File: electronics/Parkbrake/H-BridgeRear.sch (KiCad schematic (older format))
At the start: 82 parts

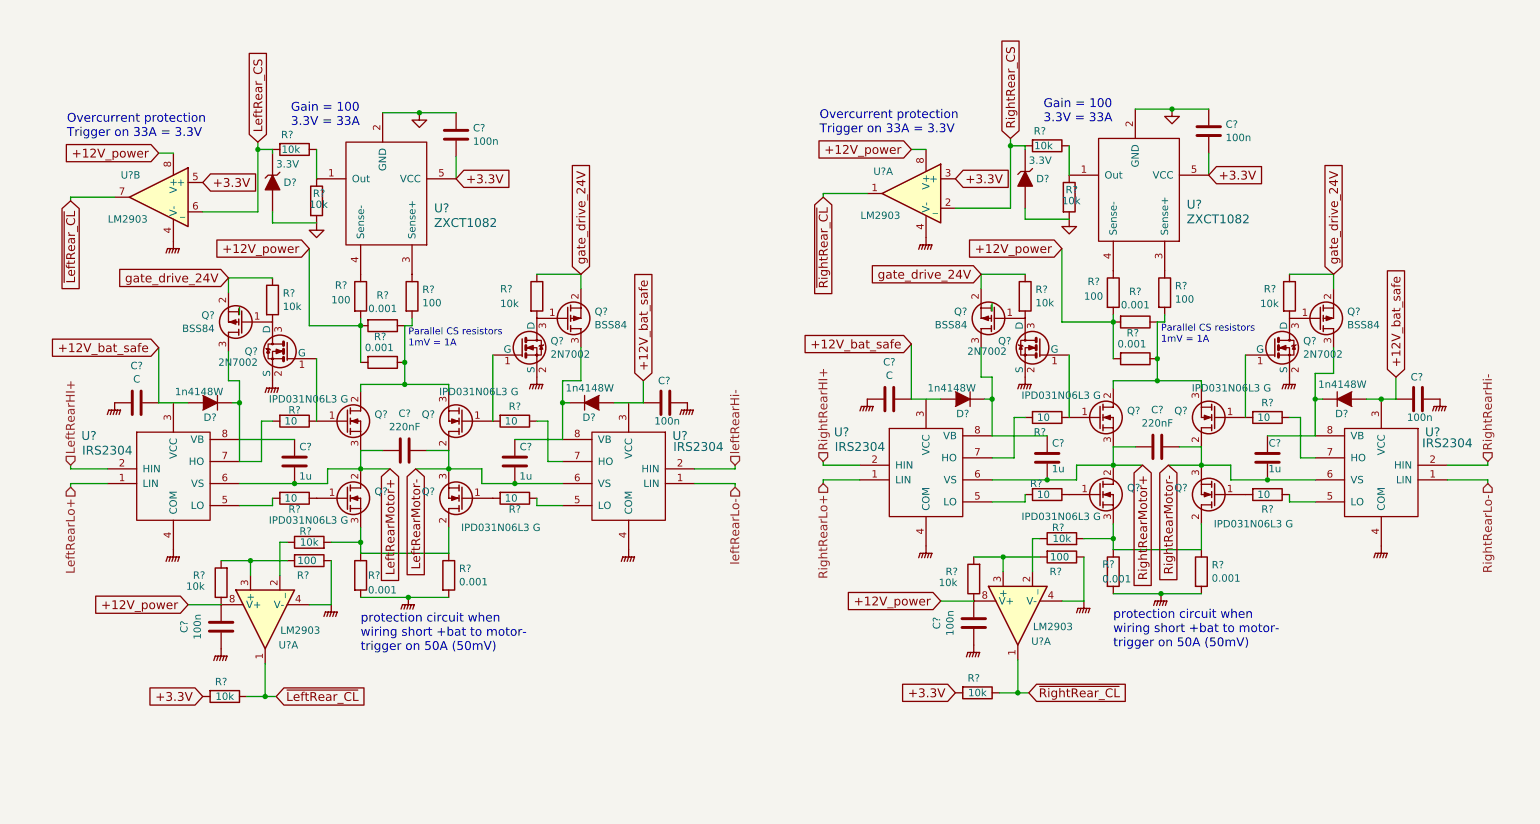
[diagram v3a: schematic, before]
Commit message: ordernr, type and footprints for all components
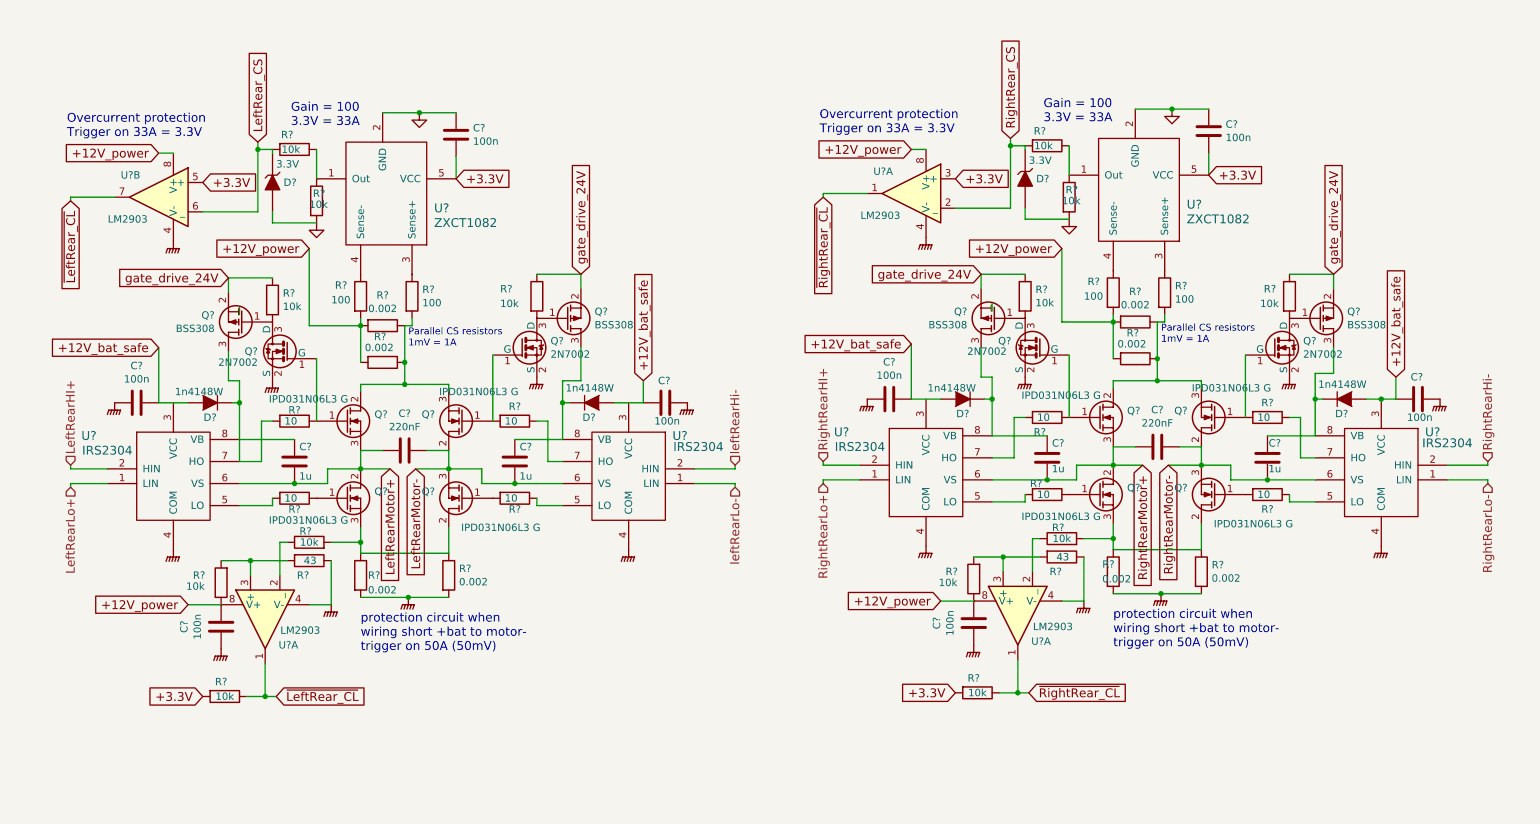
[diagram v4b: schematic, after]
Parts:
- C? (x2): footprint (none) -> Capacitors_SMD:C_1206; farnell (none) -> 2497088; part (none) -> 1206B224J500CT
- C? (x6): footprint (none) -> Capacitors_SMD:C_0805; farnell (none) -> 2496940; part (none) -> 0805B104J500CT
- C? (x4): footprint (none) -> Capacitors_SMD:C_1206; farnell (none) -> 2362126; part (none) -> GRM31MR71E105JA01L
- C? (x2): value C -> 100n; footprint (none) -> Capacitors_SMD:C_0805; farnell (none) -> 2496940; part (none) -> 0805B104J500CT
- D? (x4): footprint (none) -> Diodes_SMD:SOD-123; farnell (none) -> 2433353; part (none) -> 1N4148W-E3-08
- D? (x2): footprint (none) -> Diodes_SMD:SOD-123; farnell (none) -> 2454044; part (none) -> MMSZ4684
- Q? (x4): footprint (none) -> TO_SOT_Packages_SMD:TO-252-2Lead
- Q? (x4): footprint TO_SOT_Packages_SMD:SOT-23_Handsoldering -> TO_SOT_Packages_SMD:SOT-23
- Q? (x4): value BSS84 -> BSS308; footprint TO_SOT_Packages_SMD:SOT-23_Handsoldering -> TO_SOT_Packages_SMD:SOT-23; farnell 1510765 -> 2432719; part BSS84 -> BSS308PE H6327
- R? (x8): value 0.001 -> 0.002
- R? (x2): value 100 -> 43; footprint (none) -> Resistors_SMD:R_0805; farnell (none) -> 9333240; part (none) -> MC01W0805143R

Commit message: Make it pass DRC rule check
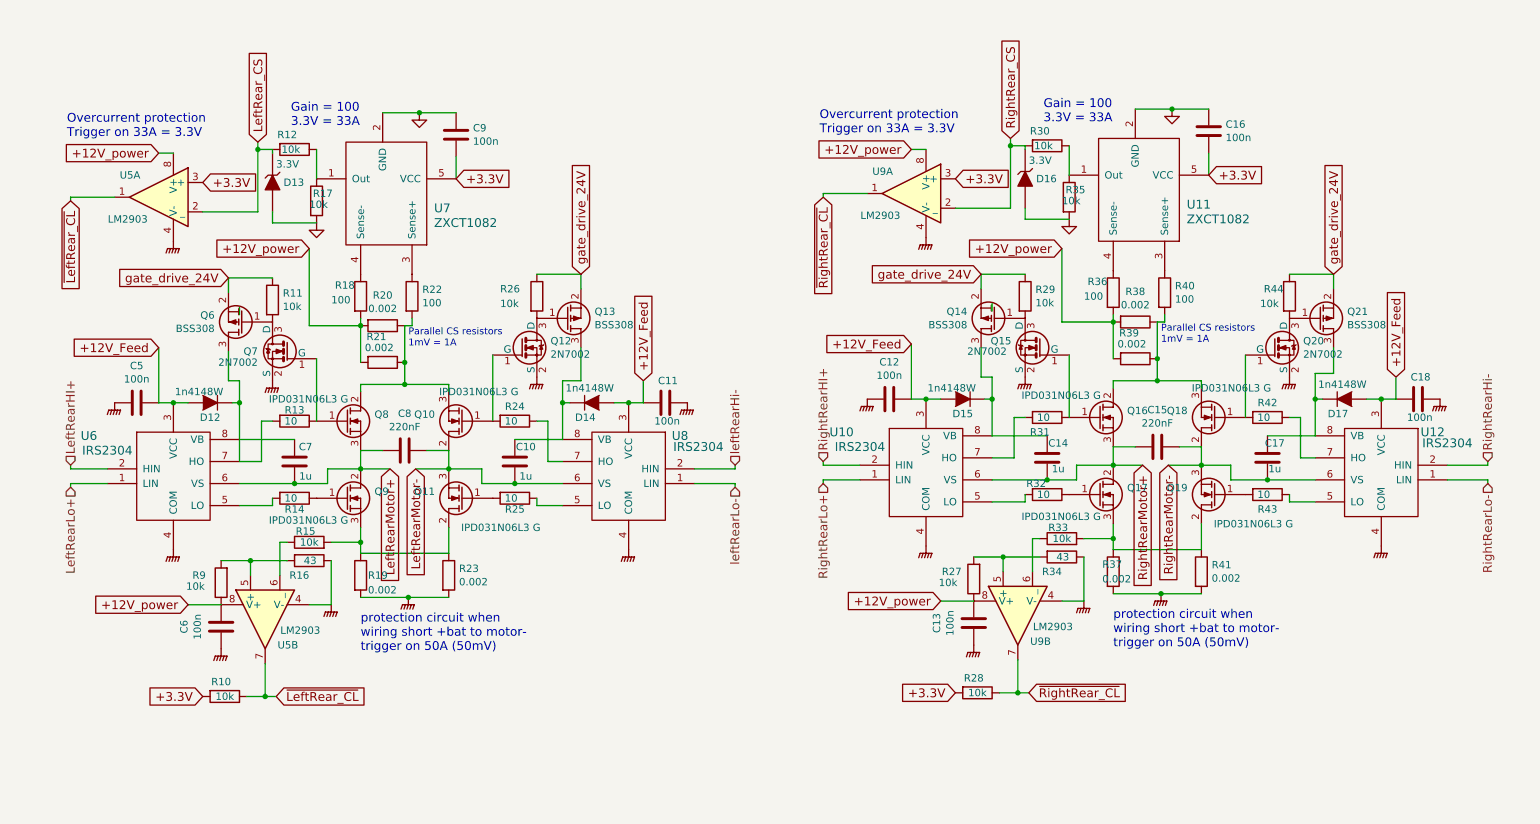
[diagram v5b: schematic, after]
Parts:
- removed C? (x5): 100n, Capacitors_SMD:C_0805, symbol C
- removed C?: 1u, Capacitors_SMD:C_1206, symbol C
- removed C?: 220nF, Capacitors_SMD:C_1206, symbol C
- removed D? (x3): 1n4148W, Diodes_SMD:SOD-123, symbol D
- removed D? (x2): 3.3V, Diodes_SMD:SOD-123, symbol ZENER
- removed Q? (x8): IPD031N06L3 G, TO_SOT_Packages_SMD:TO-252-2Lead, symbol Q_NMOS_GDS
- removed Q? (x2): 2N7002, TO_SOT_Packages_SMD:SOT-23, symbol BSS138
- removed Q? (x3): BSS308, TO_SOT_Packages_SMD:SOT-23, symbol Q_PMOS_GSD
- removed R? (x5): 0.002, Resistors_SMD:R_2512_HandSoldering, symbol R
- removed R? (x3): 100, Resistors_SMD:R_0805, symbol R
- removed R? (x9): 10k, Resistors_SMD:R_0805, symbol R
- removed R? (x2): 43, Resistors_SMD:R_0805, symbol R
- removed R? (x2): 10, Resistors_SMD:R_1206, symbol R
- removed U? (x2): ZXCT1082, TO_SOT_Packages_SMD:SOT-23-5, symbol ZXCT1082
- removed U? (x3): IRS2304, symbol IRS2304
- removed U? (x3): LM2903, symbol LM2903
- added C11, C13, C16, C5, C6: 100n, Capacitors_SMD:C_0805, symbol C
- added C15: 220nF, Capacitors_SMD:C_1206, symbol C
- added C7: 1u, Capacitors_SMD:C_1206, symbol C
- added D12, D14, D15: 1n4148W, Diodes_SMD:SOD-123, symbol D
- added D13, D16: 3.3V, Diodes_SMD:SOD-123, symbol ZENER
- added Q10, Q11, Q16, Q17, Q18, Q19, Q8, Q9: IPD031N06L3 G, TO_SOT_Packages_SMD:TO-252-2Lead, symbol Q_NMOS_GDS
- added Q13, Q21, Q6: BSS308, TO_SOT_Packages_SMD:SOT-23, symbol Q_PMOS_GSD
- added Q20, Q7: 2N7002, TO_SOT_Packages_SMD:SOT-23, symbol BSS138
- added R10, R11, R12, R17, R26, R27, R28, R33, R9: 10k, Resistors_SMD:R_0805, symbol R
- added R16, R34: 43, Resistors_SMD:R_0805, symbol R
- added R18, R22, R40: 100, Resistors_SMD:R_0805, symbol R
- added R19, R20, R21, R37, R39: 0.002, Resistors_SMD:R_2512_HandSoldering, symbol R
- added R32, R43: 10, Resistors_SMD:R_1206, symbol R
- added U10, U12, U6: IRS2304, symbol IRS2304
- added U11, U7: ZXCT1082, TO_SOT_Packages_SMD:SOT-23-5, symbol ZXCT1082
- added unit 1 of U5
- added U9: LM2903, symbol LM2903
- gave numbers to parts that had none: 28
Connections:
- net +12V_bat_safe is gone; now on net +12V_Feed: C12.1, C18.2, D17.2 (A)
- net +12V_power: now also C13.1, C6.1, R18.2, R20.2, R21.2, R27.1, R39.2, R9.1, U5.8 (V+), U9.8 (V+), U9.8 (V+)
- net +3.3V: now also C16.2, R10.2, R28.2, U11.5 (VCC), U5.3 (+), U7.5 (VCC), U9.3 (+)
- net GND: now also C16.1, D13.2 (A), D16.2 (A), R17.2, U11.2 (GND), U7.2 (GND)
- net GNDPWR: now also C11.1, C13.2, C5.2, C6.2, Q20.2 (S), Q7.2 (S), R16.1, R19.2, R34.1, R37.2, U10.4 (COM), U12.4 (COM), U5.4 (V-), U6.4 (COM), U9.4 (V-), U9.4 (V-)
- net LeftRearHI+: now also U6.2 (HIN)
- net LeftRearLo+: now also U6.1 (LIN)
- net LeftRearMotor+: now also C7.1, Q8.3 (S), Q9.2 (D), U6.6 (VS)
- net LeftRearMotor-: now also Q10.2 (D), Q11.3 (S)
- net LeftRear_CS: now also D13.1 (K), R12.2, U5.2 (_)
- net RightRearHI+: now also U10.2 (HIN)
- net RightRearHi-: now also U12.2 (HIN)
- net RightRearLo+: now also U10.1 (LIN)
- net RightRearLo-: now also U12.1 (LIN)
- net RightRearMotor+: now also C15.2, Q16.3 (S), Q17.2 (D), U10.6 (VS)
- net RightRearMotor-: now also C15.1, Q18.2 (D), Q19.3 (S), U12.6 (VS)
- net RightRear_CS: now also D16.1 (K), U9.2 (_)
- net gate_drive_24V: now also Q13.2 (S), Q21.2 (S), Q6.2 (S), R11.1, R26.1
- net ~LeftRear_CL: now also U5.7, R10.1, U5.1; no longer U5.1
- net ~RightRear_CL: now also R28.1, U9.1, U9.7
- net at R14.1: now also Q9.1 (G)
- net at R15.2, R23.1: now also Q11.2 (D), Q9.3 (S), R19.1
- net at R25.2: now also Q11.1 (G)
- net at Q12.1 (G), R24.2: now also Q10.1 (G)
- net at R13.1: now also Q7.1 (G), Q8.1 (G)
- net at R14.2: now also U6.5 (LO)
- net at R13.2: now also D12.1 (K), Q6.3 (D), U6.7 (HO)
- net at C10.2, U8.8 (VB): now also D14.1 (K), Q13.3 (D)
- net at Q12.3 (D): now also Q13.1 (G), R26.2
- net at R15.1: now also U5.6 (_); no longer U5.2 (_)
- net +12V_Feed: now reaches U8.3 (VCC)
- net +12V_Feed: now also C11.2, C5.1, D12.2 (A), D14.2 (A), D15.2 (A), U10.3 (VCC), U12.3 (VCC), U6.3 (VCC)
- net at R41.1: now also Q17.3 (S), Q19.2 (D), R33.2, R37.1
- net at R42.2: now also Q18.1 (G), Q20.1 (G)
- net at R38.1: now also Q16.2 (D), Q18.3 (S), R39.1, R40.2
- net at Q15.1 (G), R31.1: now also Q16.1 (G)
- net at R30.1, R35.1: now also U11.1 (Out)
- net at R36.1: now also U11.4 (Sense-)
- net at R31.2: now also U10.7 (HO)
- net at R42.1: now also U12.7 (HO)
- net at C17.1, D17.1 (K): now also Q21.3 (D), U12.8 (VB)
- net at R44.2: now also Q20.3 (D), Q21.1 (G)
- net at C14.2, Q14.3 (D): now also D15.1 (K), U10.8 (VB)
- new net: R16.2, R9.2, U5.5 (+)
- new net: Q10.3 (S), Q8.2 (D), R20.1, R21.1, R22.2
- new net: R12.1, R17.1, U7.1 (Out)
- new net: R22.1, U7.3 (Sense+)
- new net: R18.1, U7.4 (Sense-)
- new net: Q6.1 (G), Q7.3 (D), R11.2
- new net: C7.2, U6.8 (VB)
- new net: Q17.1 (G), R32.1
- new net: Q19.1 (G), R43.2
- new net: R40.1, U11.3 (Sense+)
- new net: R43.1, U12.5 (LO)
- new net: R32.2, U10.5 (LO)
- new net: R27.2, R34.2, U9.5 (+)
- new net: R33.1, U9.6 (_)

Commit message: More fixes and chenged components eat less boardspace
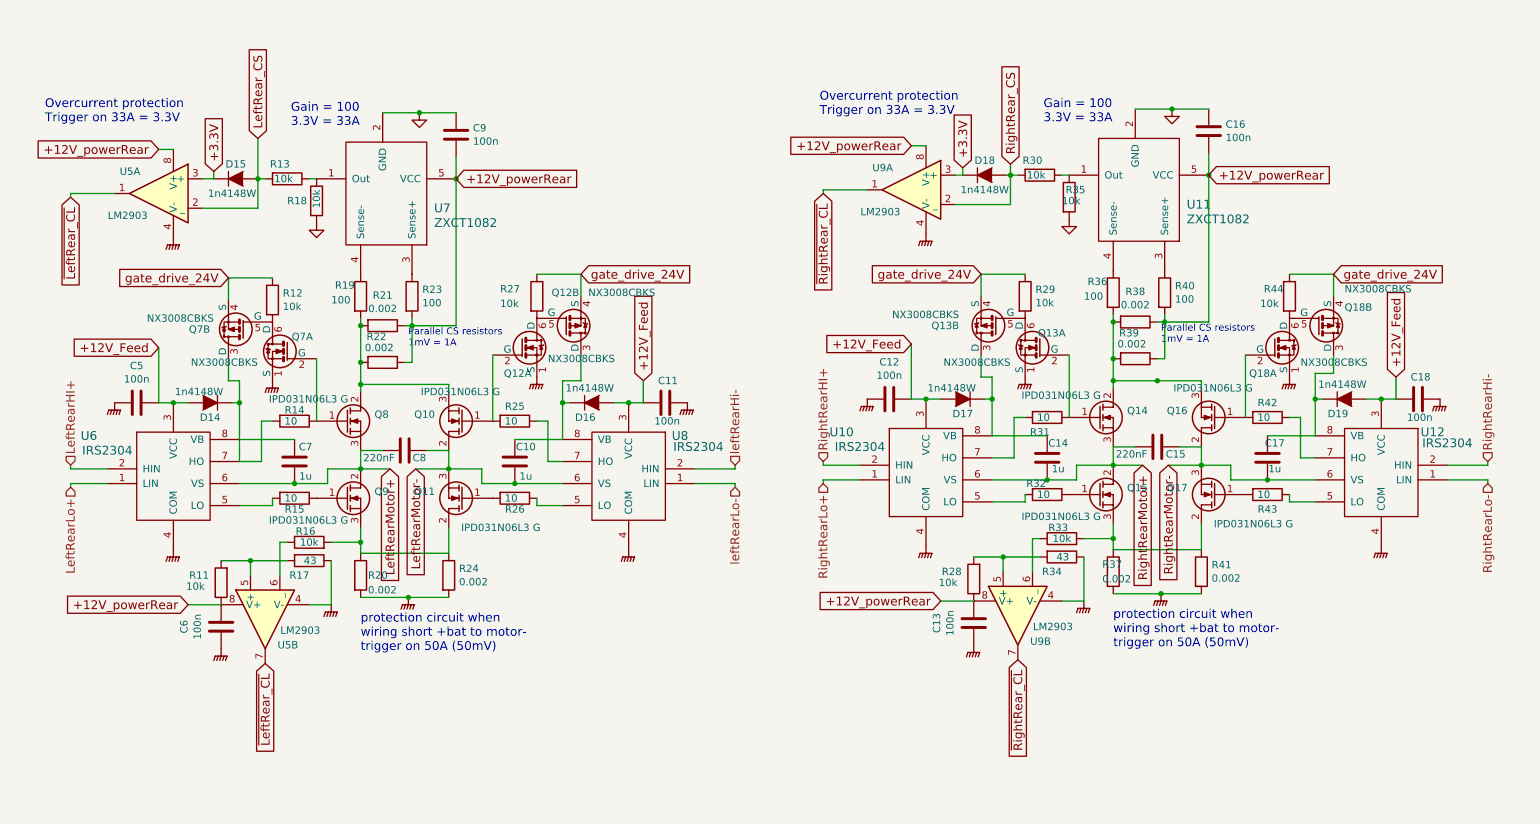
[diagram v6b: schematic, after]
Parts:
- removed D13, D16: 3.3V, Diodes_SMD:SOD-123, symbol ZENER
- removed Q12, Q15, Q20, Q7: 2N7002, TO_SOT_Packages_SMD:SOT-23, symbol BSS138
- removed Q13, Q14, Q21, Q6: BSS308, TO_SOT_Packages_SMD:SOT-23, symbol Q_PMOS_GSD
- removed R10, R28: 10k, Resistors_SMD:R_0805, symbol R
- added D15, D18: 1n4148W, Diodes_SMD:SOD-323, symbol D
- added Q12, Q13, Q18, Q7: NX3008CBKS, SOT363:SOT-363, symbol NX3008CBKS
- D14: renamed from D12; footprint Diodes_SMD:SOD-123 -> Diodes_SMD:SOD-323; farnell 2433353 -> 1466524; part 1N4148W-E3-08 -> 1N4148WS
- D16: renamed from D14; footprint Diodes_SMD:SOD-123 -> Diodes_SMD:SOD-323; farnell 2433353 -> 1466524; part 1N4148W-E3-08 -> 1N4148WS
- D17: renamed from D15; footprint Diodes_SMD:SOD-123 -> Diodes_SMD:SOD-323; farnell 2433353 -> 1466524; part 1N4148W-E3-08 -> 1N4148WS
- D19: renamed from D17; footprint Diodes_SMD:SOD-123 -> Diodes_SMD:SOD-323; farnell 2433353 -> 1466524; part 1N4148W-E3-08 -> 1N4148WS
- R20: renamed from R19; footprint Resistors_SMD:R_2512_HandSoldering -> Resistors_SMD:R_1206; farnell 2079420 -> 1621962; part LRMAT2512-R002FT4 -> ULR1S-R002FT2
- R21: renamed from R20; footprint Resistors_SMD:R_2512_HandSoldering -> Resistors_SMD:R_1206; farnell 2079420 -> 1621962; part LRMAT2512-R002FT4 -> ULR1S-R002FT2
- R22: renamed from R21; footprint Resistors_SMD:R_2512_HandSoldering -> Resistors_SMD:R_1206; farnell 2079420 -> 1621962; part LRMAT2512-R002FT4 -> ULR1S-R002FT2
- R24: renamed from R23; footprint Resistors_SMD:R_2512_HandSoldering -> Resistors_SMD:R_1206; farnell 2079420 -> 1621962; part LRMAT2512-R002FT4 -> ULR1S-R002FT2
- R37, R38, R39, R41: footprint Resistors_SMD:R_2512_HandSoldering -> Resistors_SMD:R_1206; farnell 2079420 -> 1621962; part LRMAT2512-R002FT4 -> ULR1S-R002FT2
- U10, U12, U6, U8: footprint (none) -> Housings_SOIC:SOIC-8_3.9x4.9mm_Pitch1.27mm; farnell (none) -> 1498208; part (none) -> IRS2304SPBF
- U5, U9: footprint (none) -> Housings_SSOP:TSSOP-8_4.4x3mm_Pitch0.65mm; farnell (none) -> 1094243; part (none) -> LM2903PT
- renumbered Q16 to Q14, Q17 to Q15, Q18 to Q16, Q19 to Q17, R9 to R11, R11 to R12, R12 to R13, R13 to R14, R14 to R15, R15 to R16, R16 to R17, R17 to R18, R18 to R19, R22 to R23, R24 to R25, R25 to R26, R26 to R27, R27 to R28
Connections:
- net +3.3V: now also D15.1 (K), D18.1 (K); no longer C16.2, C9.2, U11.5 (VCC), U7.5 (VCC)
- net GNDPWR: now also Q12.1 (S), Q13.1 (S), Q18.1 (S), Q7.1 (S)
- net LeftRear_CS: now also D15.2 (A)
- net RightRear_CS: now also D18.2 (A)
- net gate_drive_24V: now also Q12.4 (S), Q13.4 (S), Q18.4 (S), Q7.4 (S)
- net at Q8.1 (G), R14.1: now also Q7.2 (G)
- net at D14.1 (K), R14.2, U6.7 (HO): now also Q7.3 (D)
- net at Q10.1 (G), R25.2: now also Q12.2 (G)
- net at C10.2, D16.1 (K), U8.8 (VB): now also Q12.3 (D)
- net at R27.2: now also Q12.5 (G), Q12.6 (D)
- net +12V_powerRear: now reaches R38.1, R39.1, R40.2
- net +12V_powerRear: now also C13.1, C16.2, C6.1, C9.2, R11.1, R21.1, R22.1, R23.2, R28.1, U11.5 (VCC), U5.8 (V+), U5.8 (V+), U7.5 (VCC), U9.8 (V+), U9.8 (V+); no longer Q14.2 (D), Q16.3 (S)
- net at Q14.1 (G), R31.1: now also Q13.2 (G)
- net at Q16.1 (G), R42.2: now also Q18.2 (G)
- net at C17.1, D19.1 (K), U12.8 (VB): now also Q18.3 (D)
- net at R29.2: now also Q13.5 (G), Q13.6 (D)
- net at C14.2, D17.1 (K), U10.8 (VB): now also Q13.3 (D)
- net at R44.2: now also Q18.5 (G), Q18.6 (D)
- net at R12.2: now also Q7.5 (G), Q7.6 (D)
- removed net +12V_power: C13.1, C6.1, R11.1, R19.2, R21.2, R22.2, R28.1, R36.2, R38.2, R39.2, U5.8 (V+), U5.8 (V+), U9.8 (V+), U9.8 (V+)
- new net: Q14.2 (D), Q16.3 (S), R36.2, R38.2, R39.2
- new net: Q10.3 (S), Q8.2 (D), R19.2, R21.2, R22.2
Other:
- moved on the sheet: R13, R30, U5A, U9A

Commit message: some more work on parkbrake pcb
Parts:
- R14, R15, R25, R26, R31, R32, R42, R43: footprint Resistors_SMD:R_1206 -> Resistors_SMD:R_0805; farnell 9335790 -> 2502783; part MC0125W1206110R -> WF08P10R0FTL
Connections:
- net +12V_Feed is gone; now on net +12V_powerRear: C11.2, C12.1, C18.2, C5.1, D14.2 (A), D16.2 (A), D17.2 (A), D19.2 (A), U10.3 (VCC), U12.3 (VCC), U6.3 (VCC), U8.3 (VCC)
- net GND is gone; now on net GNDPWR: C16.1, C9.1, R18.2, R35.2, U11.2 (GND), U7.2 (GND)
- net LeftRearMotor-: now also Q10.3 (S), Q11.2 (D); no longer Q10.2 (D), Q11.3 (S)
- net RightRearMotor-: now also Q16.3 (S), Q17.2 (D); no longer Q16.2 (D), Q17.3 (S)
- net at Q9.3 (S), R16.2, R20.1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: now also Q11.3 (S); no longer Q11.2 (D)
- net at R14.2, U6.7 (HO): no longer D14.1 (K), Q7.3 (D)
- net at Q15.3 (S), R33.2, R37.1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: now also Q17.3 (S); no longer Q17.2 (D)
- net at Q14.2 (D), R36.2, R38.2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: now also Q16.2 (D); no longer Q16.3 (S)
- net at Q8.2 (D), R19.2, R21.2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: now also Q10.2 (D); no longer Q10.3 (S)
- net at C7.2, U6.8 (VB): now also D14.1 (K), Q7.3 (D)
